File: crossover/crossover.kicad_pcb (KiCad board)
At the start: 2 copper layers, 100 x 84 mm, 18 parts, among them J1 IN+, J2 IN-, J3 TW+, J4 TW-, J5 WF+, J6 WF-

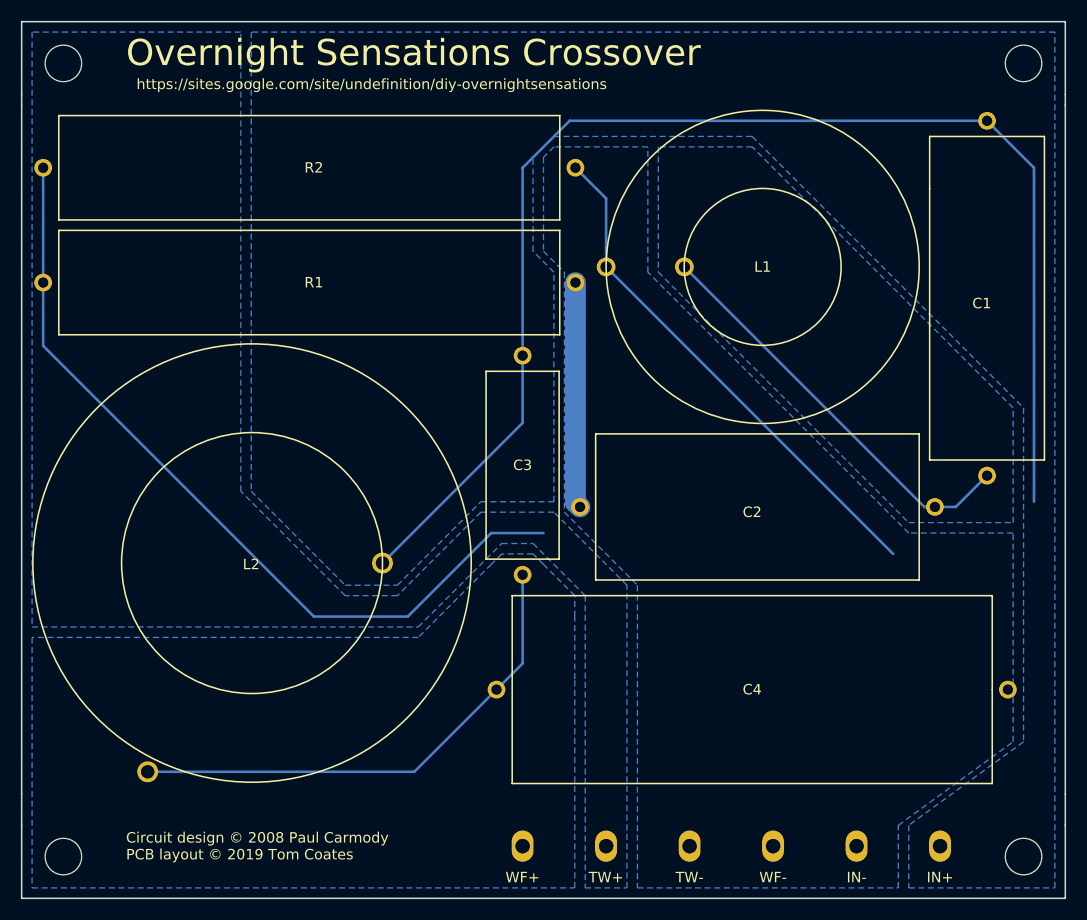
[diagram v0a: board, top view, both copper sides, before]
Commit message: Clean up traces under planes
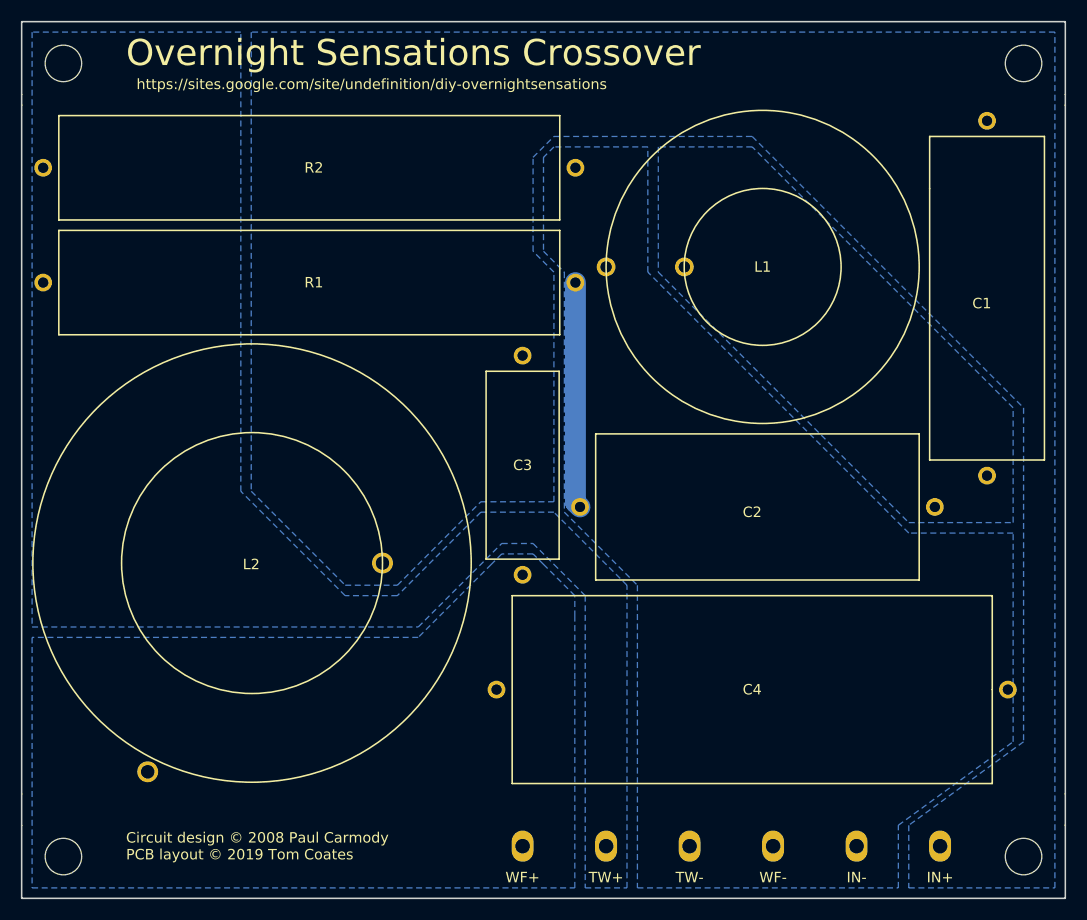
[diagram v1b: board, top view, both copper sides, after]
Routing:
- net Net-(C1-Pad2): track 128.2 -> 0.00 mm
- net Net-(J3-Pad1): track 79.1 -> 0.00 mm
- net GND: track 49.6 -> 0.00 mm
- net Net-(C3-Pad1): track 48.7 -> 0.00 mm
- net Net-(C1-Pad1): track 40.8 -> 0.00 mm
- net Net-(C2-Pad1): track 22.3 -> 21.7 mm
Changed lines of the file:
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@@
     (thickness 1.6)
     (drawings 21)
-    (tracks 28)
+    (tracks 2)
     (zones 0)
     (modules 18)
@@
     (visible_elements FFFFFF7F)
     (pcbplotparams
-      (layerselection 0x010fc_ffffffff)
+      (layerselection 0x01060_fffffffe)
       (usegerberextensions false)
       (usegerberattributes false)
@@
       (psa4output false)
       (plotreference true)
-      (plotvalue true)
+      (plotvalue false)
       (plotinvisibletext false)
       (padsonsilk false)
@@
       (outputformat 1)
       (mirror false)
-      (drillshape 1)
+      (drillshape 0)
       (scaleselection 1)
       (outputdirectory ""))
@@
   (gr_line (start 51 50) (end 51 116) (layer Edge.Cuts) (width 0.15))
   (gr_line (start 151 116) (end 151 50) (layer Edge.Cuts) (width 0.15))
-  (segment (start 137.5 88.5) (end 138.5 88.5) (width 0.25) (layer F.Cu) (net 1))
-  (segment (start 140.5 88.5) (end 143.5 85.5) (width 0.25) (layer B.Cu) (net 1))
-  (segment (start 138.5 88.5) (end 140.5 88.5) (width 0.25) (layer B.Cu) (net 1))
-  (segment (start 137.5 88.5) (end 138.5 88.5) (width 0.25) (layer B.Cu) (net 1))
-  (segment (start 114.5 65.5) (end 137.5 88.5) (width 0.25) (layer B.Cu) (net 1))
-  (segment (start 99 74) (end 99 56) (width 0.25) (layer B.Cu) (net 2))
-  (segment (start 103.5 51.5) (end 143.5 51.5) (width 0.25) (layer B.Cu) (net 2))
-  (segment (start 99 56) (end 103.5 51.5) (width 0.25) (layer B.Cu) (net 2))
-  (segment (start 99 80.450002) (end 85.575001 93.875001) (width 0.25) (layer B.Cu) (net 2))
-  (segment (start 99 74) (end 99 80.450002) (width 0.25) (layer B.Cu) (net 2))
-  (segment (start 148 56) (end 143.5 51.5) (width 0.25) (layer B.Cu) (net 2))
-  (segment (start 148 88) (end 148 56) (width 0.25) (layer B.Cu) (net 2))
-  (segment (start 104.060001 88.060001) (end 104.5 88.5) (width 0.25) (layer F.Cu) (net 3))
   (segment (start 104.060001 88.060001) (end 104.5 88.5) (width 2) (layer B.Cu) (net 3))
   (segment (start 104.060001 67) (end 104.060001 88.060001) (width 2) (layer B.Cu) (net 3))
-  (segment (start 88.624999 113.875001) (end 96.5 106) (width 0.25) (layer B.Cu) (net 4))
-  (segment (start 63.075001 113.875001) (end 88.624999 113.875001) (width 0.25) (layer B.Cu) (net 4))
-  (segment (start 99 103.5) (end 96.5 106) (width 0.25) (layer B.Cu) (net 4))
-  (segment (start 99 95) (end 99 103.5) (width 0.25) (layer B.Cu) (net 4))
-  (segment (start 107 58.939999) (end 104.060001 56) (width 0.25) (layer B.Cu) (net 5))
-  (segment (start 107 65.5) (end 107 58.939999) (width 0.25) (layer B.Cu) (net 5))
-  (segment (start 134.5 93) (end 107 65.5) (width 0.25) (layer B.Cu) (net 5))
-  (segment (start 53.060001 56) (end 53.060001 67) (width 0.25) (layer B.Cu) (net 6))
-  (segment (start 53.060001 67) (end 53.060001 73.060001) (width 0.25) (layer B.Cu) (net 6))
-  (segment (start 53.060001 73.060001) (end 79 99) (width 0.25) (layer B.Cu) (net 6))
-  (segment (start 79 99) (end 88 99) (width 0.25) (layer B.Cu) (net 6))
-  (segment (start 88 99) (end 96 91) (width 0.25) (layer B.Cu) (net 6))
-  (segment (start 96 91) (end 101 91) (width 0.25) (layer B.Cu) (net 6))
   (zone (net 4) (net_name "Net-(C3-Pad1)") (layer B.Cu) (hatch edge 0.508)
     (connect_pads (clearance 0.508))
